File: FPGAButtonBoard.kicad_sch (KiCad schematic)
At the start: 1 part

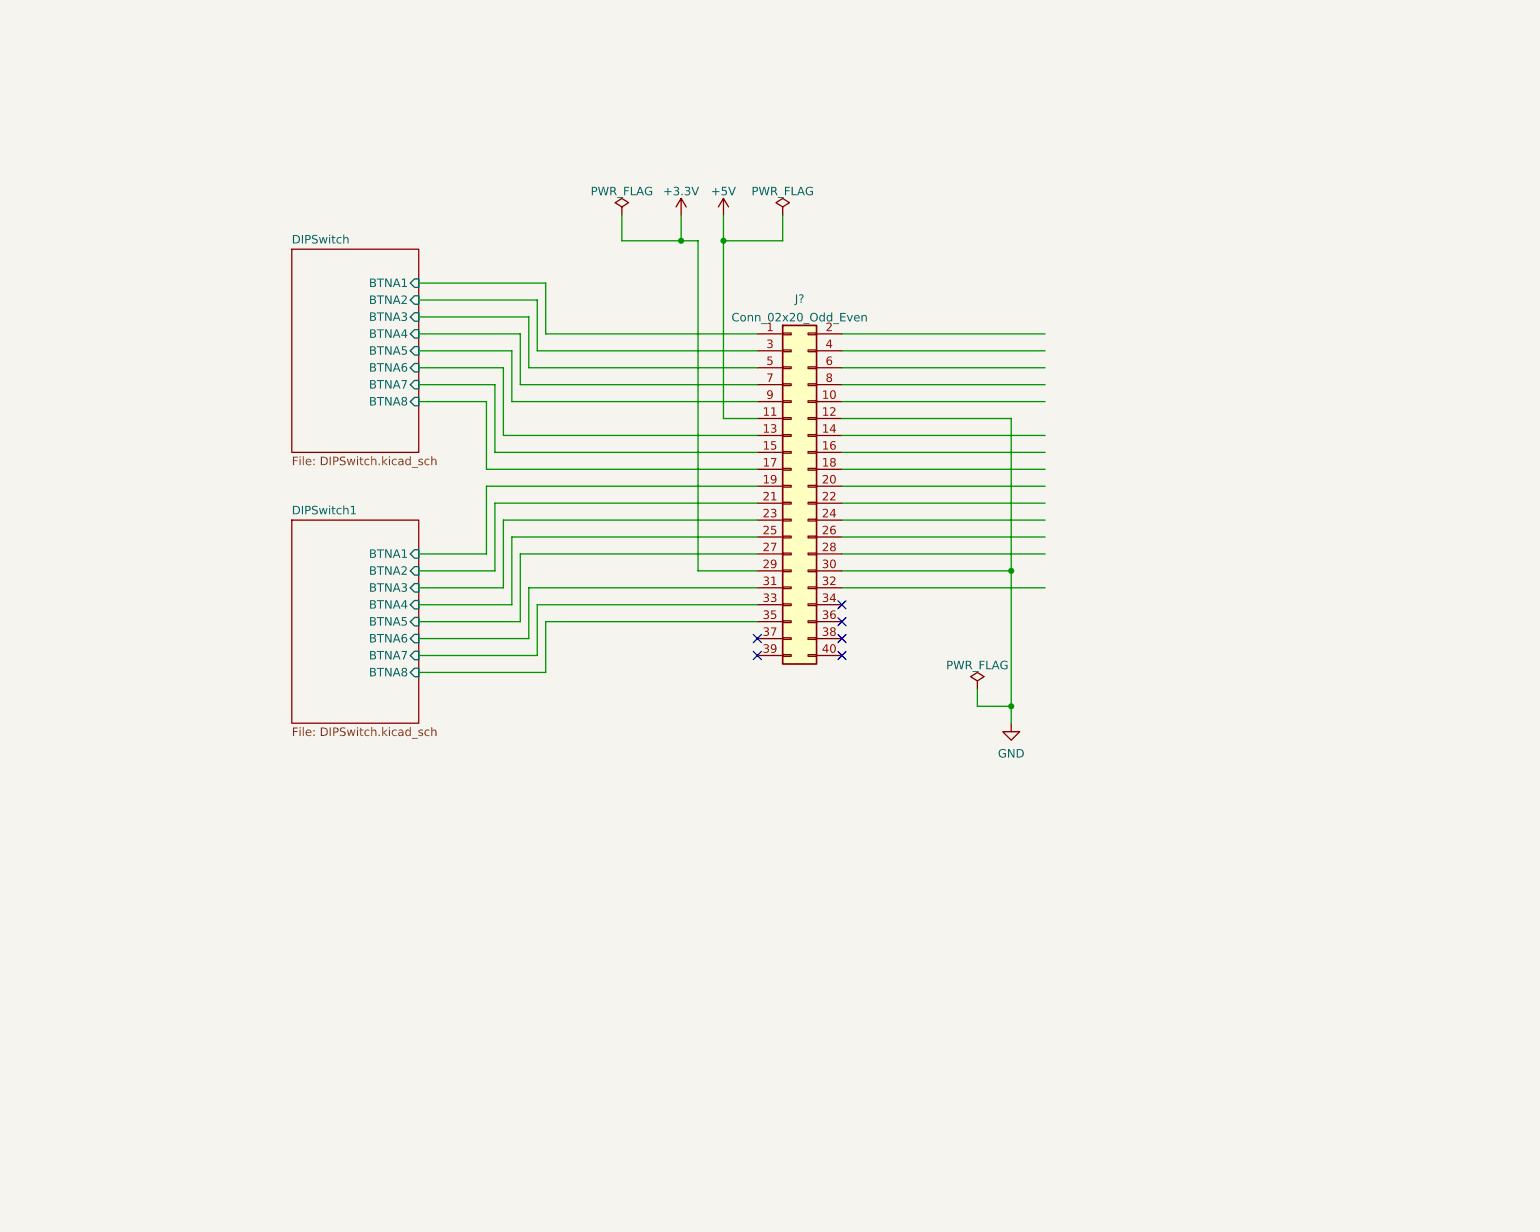
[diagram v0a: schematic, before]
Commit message: Adicionado o circuito de Debounce.
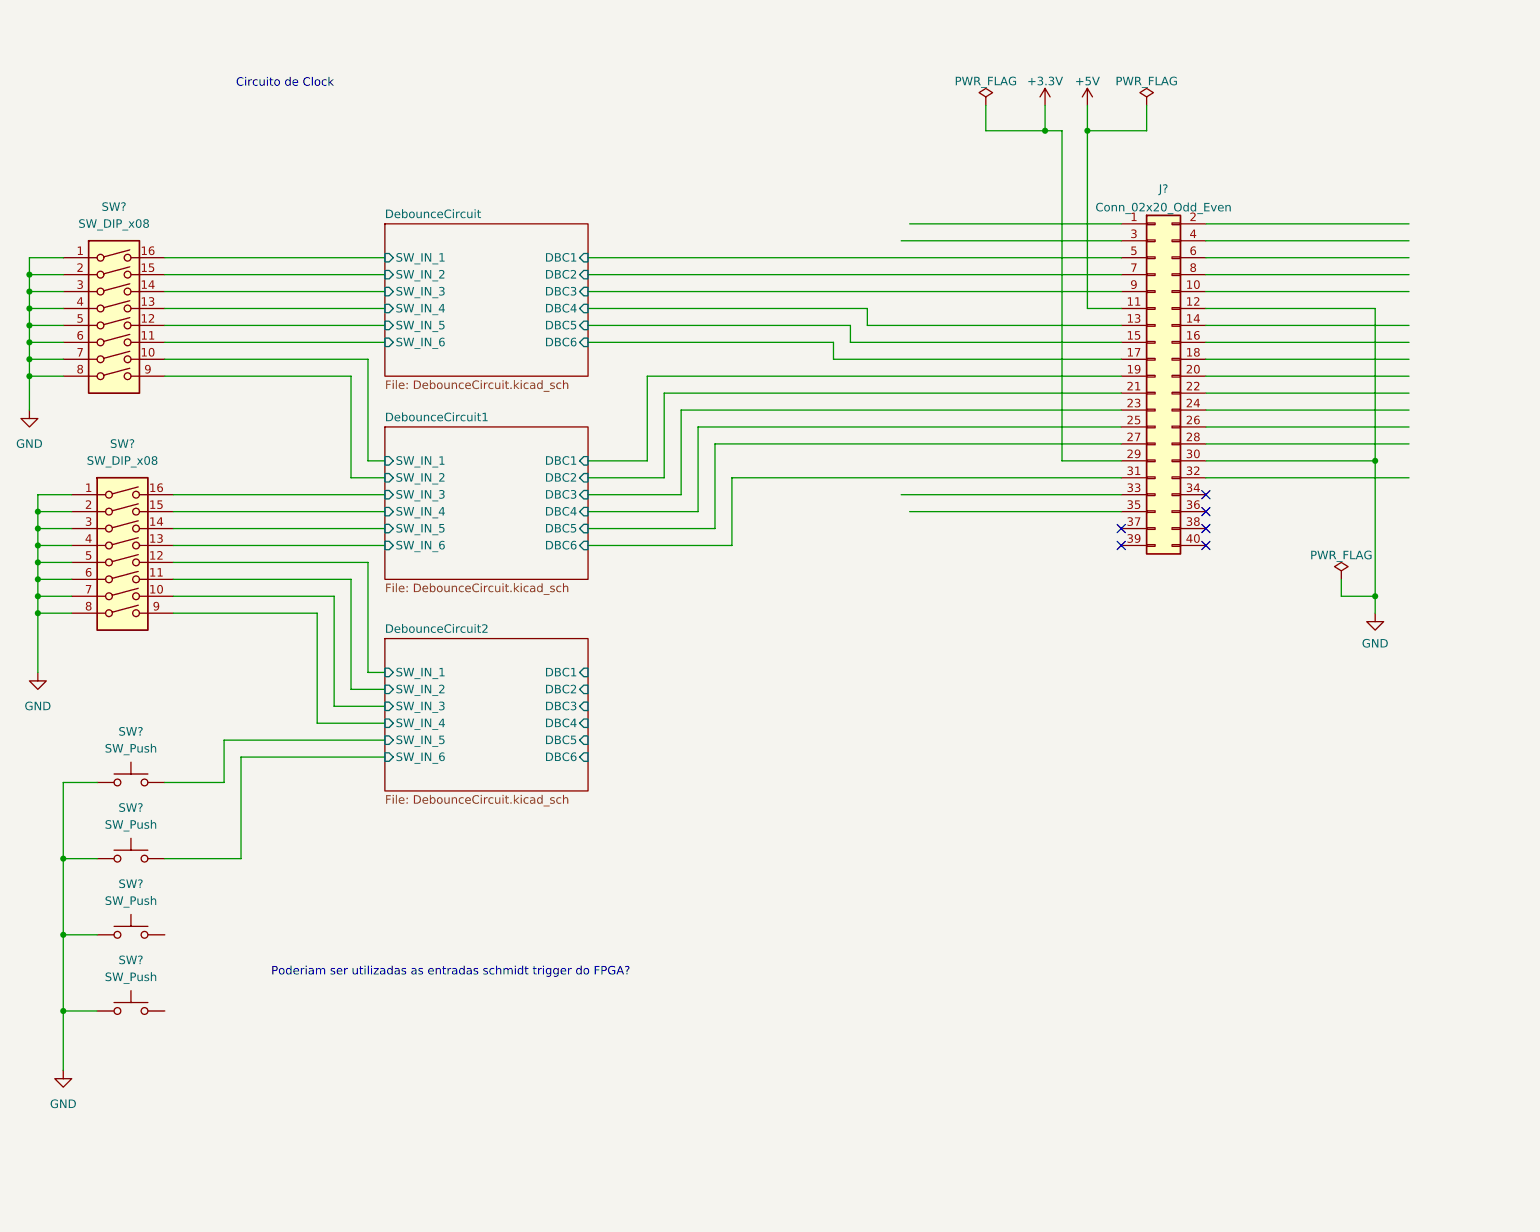
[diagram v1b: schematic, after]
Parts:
- added SW? (x4): SW_Push, symbol Switch:SW_Push
- added SW? (x2): SW_DIP_x08, symbol Switch:SW_DIP_x08
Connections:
- net GND: now also SW?.1, SW?.1, SW?.1, SW?.1, SW?.1, SW?.1, SW?.2, SW?.2, SW?.3, SW?.3, SW?.4, SW?.4, SW?.5, SW?.5, SW?.6, SW?.6, SW?.7, SW?.7, SW?.8, SW?.8
- net DIPSwitch/BTNA1: no longer names the net of J?.1 (Pin_1)
- net DIPSwitch/BTNA2: no longer names the net of J?.3 (Pin_3)
- net DIPSwitch/BTNA3 renamed DebounceCircuit/DBC1
- net DIPSwitch/BTNA4 renamed DebounceCircuit/DBC2
- net DIPSwitch/BTNA5 renamed DebounceCircuit/DBC3
- net DIPSwitch/BTNA6 renamed DebounceCircuit/DBC4
- net DIPSwitch/BTNA7 renamed DebounceCircuit/DBC5
- net DIPSwitch/BTNA8 renamed DebounceCircuit/DBC6
- net DIPSwitch1/BTNA1 renamed DebounceCircuit1/DBC1
- net DIPSwitch1/BTNA2 renamed DebounceCircuit1/DBC2
- net DIPSwitch1/BTNA3 renamed DebounceCircuit1/DBC3
- net DIPSwitch1/BTNA4 renamed DebounceCircuit1/DBC4
- net DIPSwitch1/BTNA5 renamed DebounceCircuit1/DBC5
- net DIPSwitch1/BTNA6 renamed DebounceCircuit1/DBC6
- net DIPSwitch1/BTNA7: no longer names the net of J?.33 (Pin_33)
- net DIPSwitch1/BTNA8: no longer names the net of J?.35 (Pin_35)
- new net DebounceCircuit/SW_IN_1: SW?.16
- new net DebounceCircuit/SW_IN_2: SW?.15
- new net DebounceCircuit/SW_IN_3: SW?.14
- new net DebounceCircuit/SW_IN_4: SW?.13
- new net DebounceCircuit/SW_IN_5: SW?.12
- new net DebounceCircuit/SW_IN_6: SW?.11
- new net DebounceCircuit1/SW_IN_1: SW?.10
- new net DebounceCircuit1/SW_IN_2: SW?.9
- new net DebounceCircuit1/SW_IN_3: SW?.16
- new net DebounceCircuit1/SW_IN_4: SW?.15
- new net DebounceCircuit1/SW_IN_5: SW?.14
- new net DebounceCircuit1/SW_IN_6: SW?.13
- new net DebounceCircuit2/SW_IN_1: SW?.12
- new net DebounceCircuit2/SW_IN_2: SW?.11
- new net DebounceCircuit2/SW_IN_3: SW?.10
- new net DebounceCircuit2/SW_IN_4: SW?.9
- new net DebounceCircuit2/SW_IN_5: SW?.2
- new net DebounceCircuit2/SW_IN_6: SW?.2
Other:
- removed sheet DIPSwitch
- removed sheet DIPSwitch1
- added sheet DebounceCircuit (DebounceCircuit.kicad_sch)
- added sheet DebounceCircuit1 (DebounceCircuit.kicad_sch)
- added sheet DebounceCircuit2 (DebounceCircuit.kicad_sch)
- note added: "Circuito de Clock"
- note added: "Poderiam ser utilizadas as entradas schmidt trigger do FPGA?"
- moved on the sheet: J?

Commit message: Adicionado os botões e clock. Adicionada interface com o Analog Discovery 2.
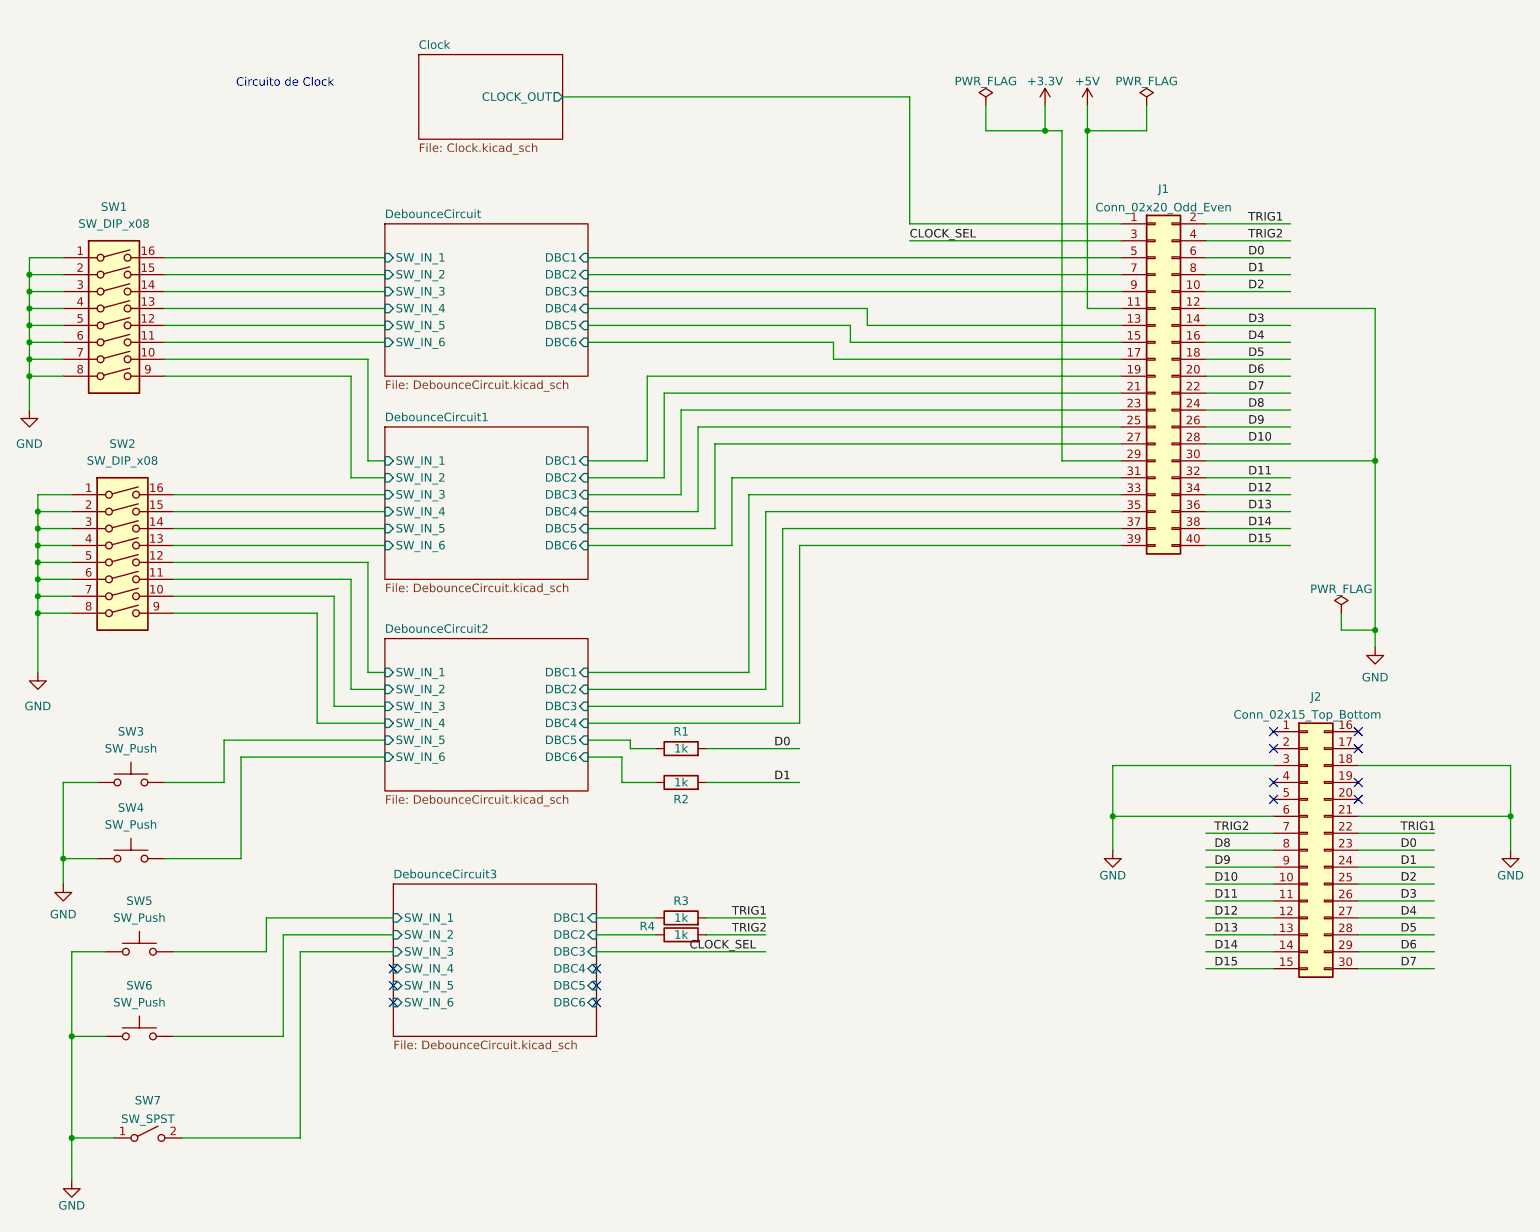
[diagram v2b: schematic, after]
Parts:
- removed SW? (x2): SW_Push, symbol Switch:SW_Push
- added J2: Conn_02x15_Top_Bottom, symbol Connector_Generic:Conn_02x15_Top_Bottom
- added R1, R2, R3, R4: 1k, symbol Device:R
- added SW5, SW6: SW_Push, symbol Switch:SW_Push
- added SW7: SW_SPST, symbol Switch:SW_SPST
- gave numbers to parts that had none: 5
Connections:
- net DebounceCircuit2/DBC1: now also J1.33 (Pin_33)
- net DebounceCircuit2/DBC2: now also J1.35 (Pin_35)
- net DebounceCircuit2/DBC3: now also J1.37 (Pin_37)
- net DebounceCircuit2/DBC4: now also J1.39 (Pin_39)
- net DebounceCircuit2/DBC5: now also R1.1
- net DebounceCircuit2/DBC6: now also R2.1
- net GND: now also J2.18 (Pin_18), J2.21 (Pin_21), J2.3 (Pin_3), J2.6 (Pin_6), SW5.1, SW6.1, SW7.1 (A)
- net Clock/CLOCK_OUT: now reaches J1.1 (Pin_1)
- net D2: now reaches J1.10 (Pin_10)
- net D2: now also J2.25 (Pin_25)
- net D3: now reaches J1.14 (Pin_14)
- net D3: now also J2.26 (Pin_26)
- net D4: now reaches J1.16 (Pin_16)
- net D4: now also J2.27 (Pin_27)
- net D5: now reaches J1.18 (Pin_18)
- net D5: now also J2.28 (Pin_28)
- net TRIG1: now reaches J1.2 (Pin_2)
- net TRIG1: now also J2.22 (Pin_22), R3.2
- net D6: now reaches J1.20 (Pin_20)
- net D6: now also J2.29 (Pin_29)
- net D7: now reaches J1.22 (Pin_22)
- net D7: now also J2.30 (Pin_30)
- net D8: now reaches J1.24 (Pin_24)
- net D8: now also J2.8 (Pin_8)
- net D9: now reaches J1.26 (Pin_26)
- net D9: now also J2.9 (Pin_9)
- net D10: now reaches J1.28 (Pin_28)
- net D10: now also J2.10 (Pin_10)
- net CLOCK_SEL: now reaches J1.3 (Pin_3)
- net D11: now reaches J1.32 (Pin_32)
- net D11: now also J2.11 (Pin_11)
- net D12: now reaches J1.34 (Pin_34)
- net D12: now also J2.12 (Pin_12)
- net D13: now reaches J1.36 (Pin_36)
- net D13: now also J2.13 (Pin_13)
- net D14: now reaches J1.38 (Pin_38)
- net D14: now also J2.14 (Pin_14)
- net TRIG2: now reaches J1.4 (Pin_4)
- net TRIG2: now also J2.7 (Pin_7), R4.2
- net D15: now reaches J1.40 (Pin_40)
- net D15: now also J2.15 (Pin_15)
- net D0: now reaches J1.6 (Pin_6)
- net D0: now also J2.23 (Pin_23), R1.2
- net D1: now reaches J1.8 (Pin_8)
- net D1: now also J2.24 (Pin_24), R2.2
- new net DebounceCircuit3/DBC1: R3.1
- new net DebounceCircuit3/DBC2: R4.1
- new net DebounceCircuit3/SW_IN_1: SW5.2
- new net DebounceCircuit3/SW_IN_2: SW6.2
- new net DebounceCircuit3/SW_IN_3: SW7.2 (B)
- no-connect marks 6 -> 14
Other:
- added sheet Clock (Clock.kicad_sch)
- added sheet DebounceCircuit3 (DebounceCircuit.kicad_sch)
- note removed: "Poderiam ser utilizadas as entradas schmidt trigger do FPGA?"
- company: (none) -> Ailton Luiz Dias Siqueira Junior
- title: (none) -> FGPA Input Board

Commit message: Removido o circuito debounce do dipswitch
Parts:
- removed J2: Conn_02x15_Top_Bottom, symbol Connector_Generic:Conn_02x15_Top_Bottom
- added J2: Analog Discovery 2, Connector_IDC:IDC-Header_2x15_P2.54mm_Vertical, symbol Connector_Generic:Conn_02x15_Odd_Even
- added R10, R11, R12, R13, R14, R15, R16, R5, R6, R7, R8, R9: 10k, Resistor_THT:R_Axial_DIN0207_L6.3mm_D2.5mm_P7.62mm_Horizontal, symbol Device:R
- added R17, R18, R19, R20, R21: 1k, Resistor_THT:R_Axial_DIN0207_L6.3mm_D2.5mm_P7.62mm_Horizontal, symbol Device:R
- added SW7: SW_Push, Button_Switch_THT:SW_PUSH-12mm_Wuerth-430476085716, symbol Switch:SW_Push
- R1, R2, R3, R4: value 1k -> 10k; footprint (none) -> Resistor_THT:R_Axial_DIN0207_L6.3mm_D2.5mm_P7.62mm_Horizontal
- SW1, SW2: footprint (none) -> Button_Switch_THT:SW_DIP_SPSTx08_Slide_6.7x21.88mm_W7.62mm_P2.54mm_LowProfile
- SW3, SW4, SW5, SW6: footprint (none) -> Button_Switch_THT:SW_PUSH-12mm_Wuerth-430476085716
- SW8: renamed from SW7; footprint (none) -> Button_Switch_THT:SW_PUSH_6mm
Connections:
- net DebounceCircuit/SW_IN_1 is gone; now on an unnamed net: SW1.16
- net DebounceCircuit/SW_IN_2 is gone; now on an unnamed net: SW1.15
- net DebounceCircuit/SW_IN_3 is gone; now on an unnamed net: SW1.14
- net DebounceCircuit/SW_IN_4 is gone; now on an unnamed net: SW1.13
- net DebounceCircuit/SW_IN_5 is gone; now on an unnamed net: SW1.12
- net DebounceCircuit/SW_IN_6 is gone; now on an unnamed net: SW1.11
- net DebounceCircuit1/SW_IN_1 is gone; now on an unnamed net: SW1.10
- net DebounceCircuit1/SW_IN_2 is gone; now on an unnamed net: SW1.9
- net DebounceCircuit1/SW_IN_3 is gone; now on an unnamed net: SW2.16
- net DebounceCircuit1/SW_IN_4 is gone; now on an unnamed net: SW2.15
- net DebounceCircuit1/SW_IN_5 is gone; now on an unnamed net: SW2.14
- net DebounceCircuit1/SW_IN_6 is gone; now on an unnamed net: SW2.13
- net DebounceCircuit2/DBC5 is gone; now on net +3V3: R1.1
- net DebounceCircuit2/DBC6 is gone; now on net +3V3: R2.1
- net DebounceCircuit2/SW_IN_1 is gone; now on an unnamed net: SW2.12
- net DebounceCircuit2/SW_IN_2 is gone; now on an unnamed net: SW2.11
- net DebounceCircuit2/SW_IN_3 is gone; now on an unnamed net: SW2.10
- net DebounceCircuit2/SW_IN_4 is gone; now on an unnamed net: SW2.9
- net DebounceCircuit2/SW_IN_5 is gone; now on net DebounceCircuit3/SW_IN_1: SW3.2
- net DebounceCircuit2/SW_IN_6 is gone; now on net DebounceCircuit3/SW_IN_2: SW4.2
- net +3V3: now also R3.1, R4.1, R10.1, R11.1, R12.1, R13.1, R14.1, R15.1, R16.1, R5.1, R6.1, R7.1, R8.1, R9.1
- net D0: now also J2.15 (Pin_15), R19.2; no longer R1.2
- net D1: now also J2.13 (Pin_13), R20.2; no longer R2.2
- net D10: now also J2.12 (Pin_12)
- net D11: now also J2.10 (Pin_10)
- net D12: now also J2.8 (Pin_8)
- net D13: now also J2.6 (Pin_6)
- net D14: now also J2.4 (Pin_4)
- net D15: now also J2.2 (Pin_2)
- net D2: now also J2.11 (Pin_11), R21.2
- net D3: now also J2.9 (Pin_9)
- net D4: now also J2.7 (Pin_7)
- net D5: now also J2.5 (Pin_5)
- net D6: now also J2.3 (Pin_3)
- net D7: now also J2.1 (Pin_1)
- net D8: now also J2.16 (Pin_16)
- net D9: now also J2.14 (Pin_14)
- net DebounceCircuit3/DBC1: now also R17.1; no longer R3.1
- net DebounceCircuit3/DBC2: now also R18.1; no longer R4.1
- net DebounceCircuit3/DBC4: now also R20.1
- net DebounceCircuit3/DBC5: now also R21.1
- net DebounceCircuit3/SW_IN_1: no longer SW5.2
- net DebounceCircuit3/SW_IN_2: no longer SW6.2
- net DebounceCircuit3/SW_IN_3: now also SW5.2; no longer SW8.2 (B)
- net DebounceCircuit3/SW_IN_4: now also SW6.2
- net DebounceCircuit3/SW_IN_5: now also SW7.2
- net DebounceCircuit3/SW_IN_6: now also SW8.2 (B)
- net GND: now also J2.19 (Pin_19), J2.20 (Pin_20), J2.25 (Pin_25), J2.26 (Pin_26), SW7.1
- net TRIG1: now also J1.4 (Pin_4), J2.17 (Pin_17), R17.2; no longer J1.2 (Pin_2), R3.2
- net TRIG2: now also J1.2 (Pin_2), J2.18 (Pin_18), R18.2; no longer J1.4 (Pin_4), R4.2
- net DebounceCircuit/DBC1: no longer names the net of J1.5 (Pin_5)
- net DebounceCircuit/DBC1: now also R1.2
- net DebounceCircuit/DBC2: no longer names the net of J1.7 (Pin_7)
- net DebounceCircuit/DBC2: now also R3.2
- net DebounceCircuit/DBC3: no longer names the net of J1.9 (Pin_9)
- net DebounceCircuit/DBC3: now also R5.2
- net DebounceCircuit/DBC4: no longer names the net of J1.13 (Pin_13)
- net DebounceCircuit/DBC4: now also R7.2
- net DebounceCircuit/DBC5: no longer names the net of J1.15 (Pin_15)
- net DebounceCircuit/DBC5: now also R9.2
- net DebounceCircuit/DBC6: no longer names the net of J1.17 (Pin_17)
- net DebounceCircuit/DBC6: now also R11.2
- net DebounceCircuit1/DBC1: no longer names the net of J1.19 (Pin_19)
- net DebounceCircuit1/DBC1: now also R13.2
- net DebounceCircuit1/DBC2: no longer names the net of J1.21 (Pin_21)
- net DebounceCircuit1/DBC2: now also R15.2
- net DebounceCircuit1/DBC3: no longer names the net of J1.23 (Pin_23)
- net DebounceCircuit1/DBC3: now also R2.2
- net DebounceCircuit1/DBC4: no longer names the net of J1.25 (Pin_25)
- net DebounceCircuit1/DBC4: now also R4.2
- net DebounceCircuit1/DBC5: no longer names the net of J1.27 (Pin_27)
- net DebounceCircuit1/DBC5: now also R6.2
- net DebounceCircuit1/DBC6: no longer names the net of J1.31 (Pin_31)
- net DebounceCircuit1/DBC6: now also R8.2
- net DebounceCircuit2/DBC1: no longer names the net of J1.33 (Pin_33)
- net DebounceCircuit2/DBC1: now also R10.2
- net DebounceCircuit2/DBC2: no longer names the net of J1.35 (Pin_35)
- net DebounceCircuit2/DBC2: now also R12.2
- net DebounceCircuit2/DBC3: no longer names the net of J1.37 (Pin_37)
- net DebounceCircuit2/DBC3: now also R14.2
- net DebounceCircuit2/DBC4: no longer names the net of J1.39 (Pin_39)
- net DebounceCircuit2/DBC4: now also R16.2
- new net DebounceCircuit3/DBC3: R19.1
- no-connect marks 14 -> 8
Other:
- removed sheet DebounceCircuit
- removed sheet DebounceCircuit1
- removed sheet DebounceCircuit2
- note removed: "Circuito de Clock"
- moved on the sheet: SW2, SW3, SW4, SW8
